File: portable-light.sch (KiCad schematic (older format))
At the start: 97 parts, among them J1 Conn_01x08, J2 Prog, Q1 MMBT2222A, Q2 MMBT2222A, Q3 MMBT2222A, Q4 MMBT2222A, Q5 MMBT2222A, Q6 PHD45N03LTA, Q7 PHD45N03LTA, Q8 MMBT2222A, U1 ATmega88PA-AU, U2 L78L05_SOT89, U3 LTC1733EMSEPBF, X1 LOAD, Y1 Crystal

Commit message: Schematics and PCB layout complete
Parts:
- removed C4: 100n, Capacitor_SMD:C_1206_3216Metric_Pad1.42x1.75mm_HandSolder, symbol Device:C_Small
- removed R26: 1MEG, Resistor_THT:R_Axial_DIN0309_L9.0mm_D3.2mm_P12.70mm_Horizontal, symbol Device:R_Small
- added J3: Charger, Connector_PinHeader_2.54mm:PinHeader_1x02_P2.54mm_Vertical, symbol Connector_Generic:Conn_01x02
- added JP1: Jumper_2_Open, Jumper:SolderJumper-2_P1.3mm_Open_RoundedPad1.0x1.5mm, symbol Jumper:Jumper_2_Open
- added NT1, NT2: Net-Tie_2, NetTie:NetTie-2_SMD_Pad0.5mm, symbol Device:Net-Tie_2
- BT1: footprint Connector_PinHeader_1.00mm:PinHeader_1x02_P1.00mm_Vertical -> Connector_PinHeader_2.54mm:PinHeader_1x02_P2.54mm_Vertical
- C4: renamed from C5; value 100n -> 330n
- R25: value 1MEG -> 500K
- renumbered C11 to C10, C12 to C11, C13 to C12, C14 to C13, C15 to C14, C16 to C15, C17 to C16, C18 to C17, C20 to C18, C21 to C19, C19 to C20, C23 to C21, C24 to C23, C25 to C24, C26 to C25, C6 to C5, C7 to C6, C8 to C7, C9 to C8, C10 to C9, X1 to J4, JP1 to JP2, R27 to R26, R28 to R27, R29 to R28, R30 to R29, R31 to R30, R32 to R31, R33 to R32, R34 to R33, R35 to R34, R36 to R35, R37 to R36, R38 to R37, R39 to R38, R40 to R39, R41 to R40, R42 to R41, R43 to R42, R44 to R43
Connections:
- net +BATT: now also U3.8 (SEL)
- net GND: now also NT1.1, NT2.1; no longer C13.2, C14.2
- net GNDA: now also NT2.2
- net GNDPWR: now also C13.2, C14.2, J3.2 (Pin_2), NT1.2
- net VDC: now also J3.1 (Pin_1); no longer U3.8 (SEL)
- net high_mos: now also U1.1 (PD3); no longer J2.5 (Pin_5), U1.15 (PB3)
- net low_mos: now also JP1.2 (B); no longer U1.1 (PD3)
- net oc1a: now also U1.12 (PB0); no longer U1.13 (PB1)
- net prog_pulldown: now also U1.32 (PD2); no longer U1.31 (PD1)
- net prog_pullup: now also U1.31 (PD1); no longer U1.32 (PD2)
- net pump-in: now also U1.13 (PB1); no longer U1.12 (PB0)
- new net mosi: J2.5 (Pin_5), JP1.1 (A), U1.15 (PB3)
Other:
- note added: "Power"
- moved on the sheet: BT1, C1, C10, C11, C12, C13, C14, C15, C16, C17, C18, C19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

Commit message: commit before checkout
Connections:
- net +BATT: no longer U3.8 (SEL)
- net VDC: now also U3.8 (SEL)
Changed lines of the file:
@@
 L power:+BATT #PWR041
 U 1 1 5F1C71D9
-P 9800 1050
-F 0 "#PWR041" H 9800 900 50  0001 C CNN
-F 1 "+BATT" H 9800 1200 50  0000 C CNN
-F 2 "" H 9800 1050 50  0001 C CNN
-F 3 "" H 9800 1050 50  0001 C CNN
-	1    9800 1050
+P 9800 1300
+F 0 "#PWR041" H 9800 1150 50  0001 C CNN
+F 1 "+BATT" H 9800 1450 50  0000 C CNN
+F 2 "" H 9800 1300 50  0001 C CNN
+F 3 "" H 9800 1300 50  0001 C CNN
+	1    9800 1300
 	1    0    0    -1
 $EndComp
 Wire Wire Line
 	9300 1600 9800 1600
-Wire Wire Line
-	9800 1600 9800 1050
-Wire Wire Line
-	9550 1700 9550 1050
 Wire Wire Line
 	9300 1700 9550 1700
@@
 	3750 2400 3950 2400
 $Comp
-L power:+BATT #PWR040
-U 1 1 5F20B594
-P 9550 1050
-F 0 "#PWR040" H 9550 900 50  0001 C CNN
-F 1 "+BATT" H 9500 1200 50  0000 C CNN
-F 2 "" H 9550 1050 50  0001 C CNN
-F 3 "" H 9550 1050 50  0001 C CNN
-	1    9550 1050
-	1    0    0    -1
-$EndComp
-$Comp
 L Connector_Generic:Conn_01x02 J3
 U 1 1 5F22ABC0
@@
 Text Notes 4450 7500 0    157  ~ 31
 Power
+$Comp
+L power:VDC #PWR?
+U 1 1 5F1D8884
+P 9550 1300
+F 0 "#PWR?" H 9550 1200 50  0001 C CNN
+F 1 "VDC" H 9550 1450 50  0000 C CNN
+F 2 "" H 9550 1300 50  0001 C CNN
+F 3 "" H 9550 1300 50  0001 C CNN
+	1    9550 1300
+	1    0    0    -1
+$EndComp
+Wire Wire Line
+	9550 1700 9550 1300
+Wire Wire Line
+	9800 1600 9800 1300
 $EndSCHEMATC

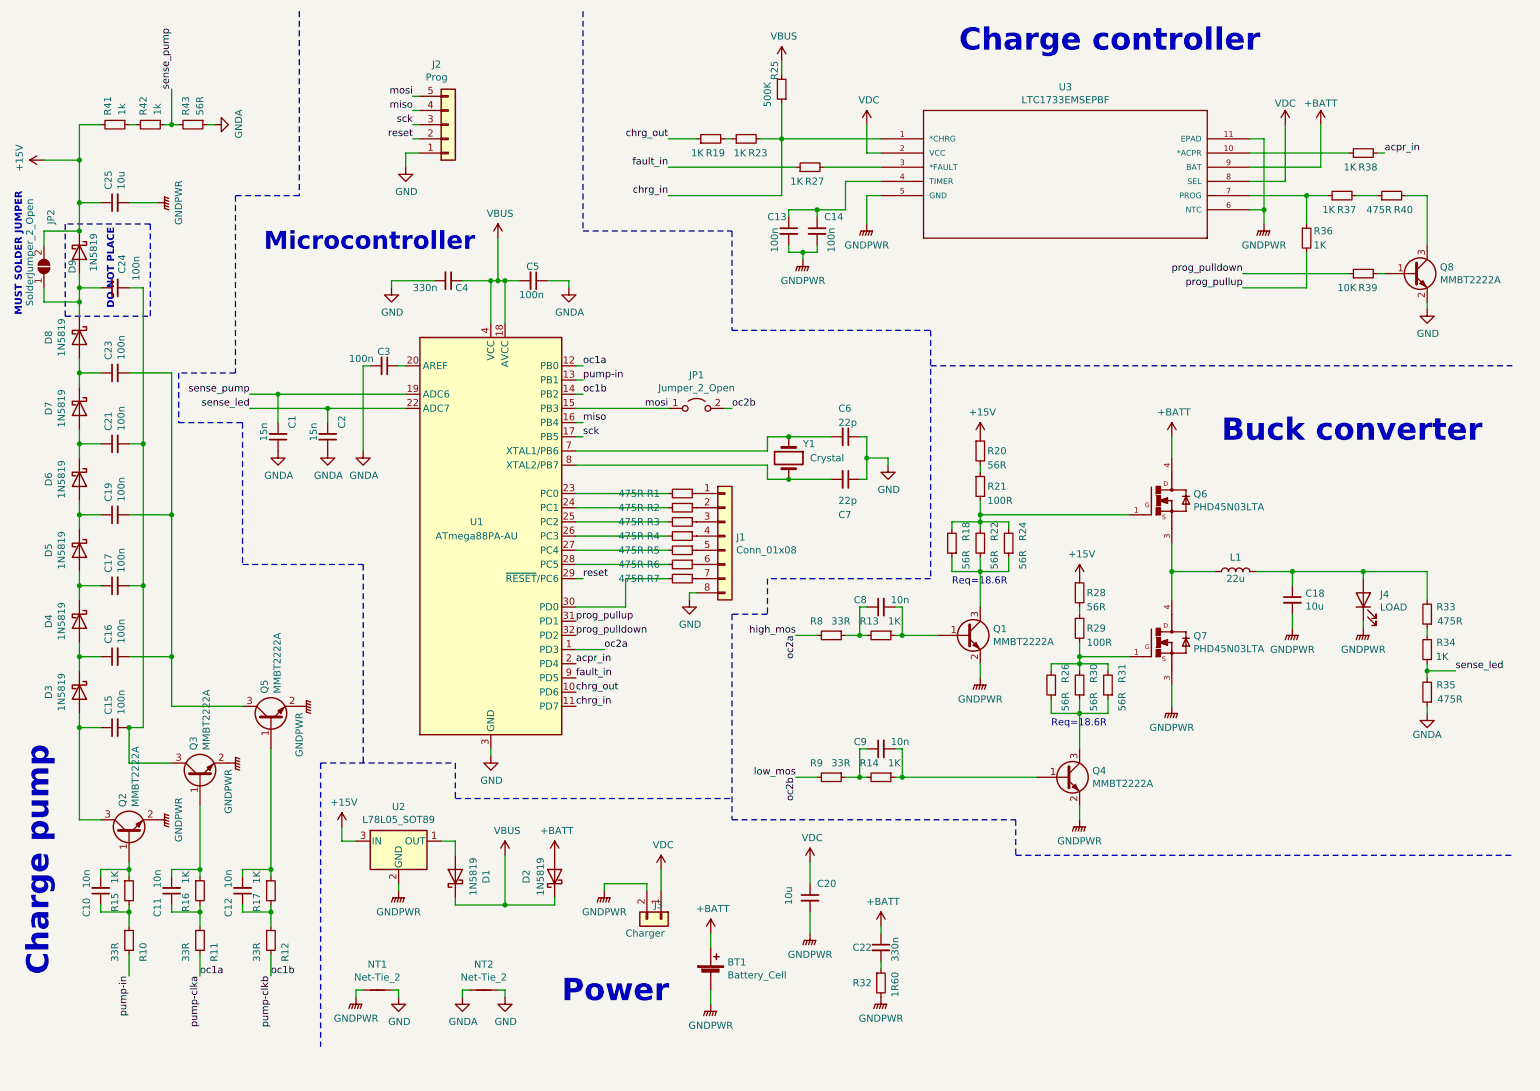
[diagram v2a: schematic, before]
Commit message: AVR Charge-pump bug fixed
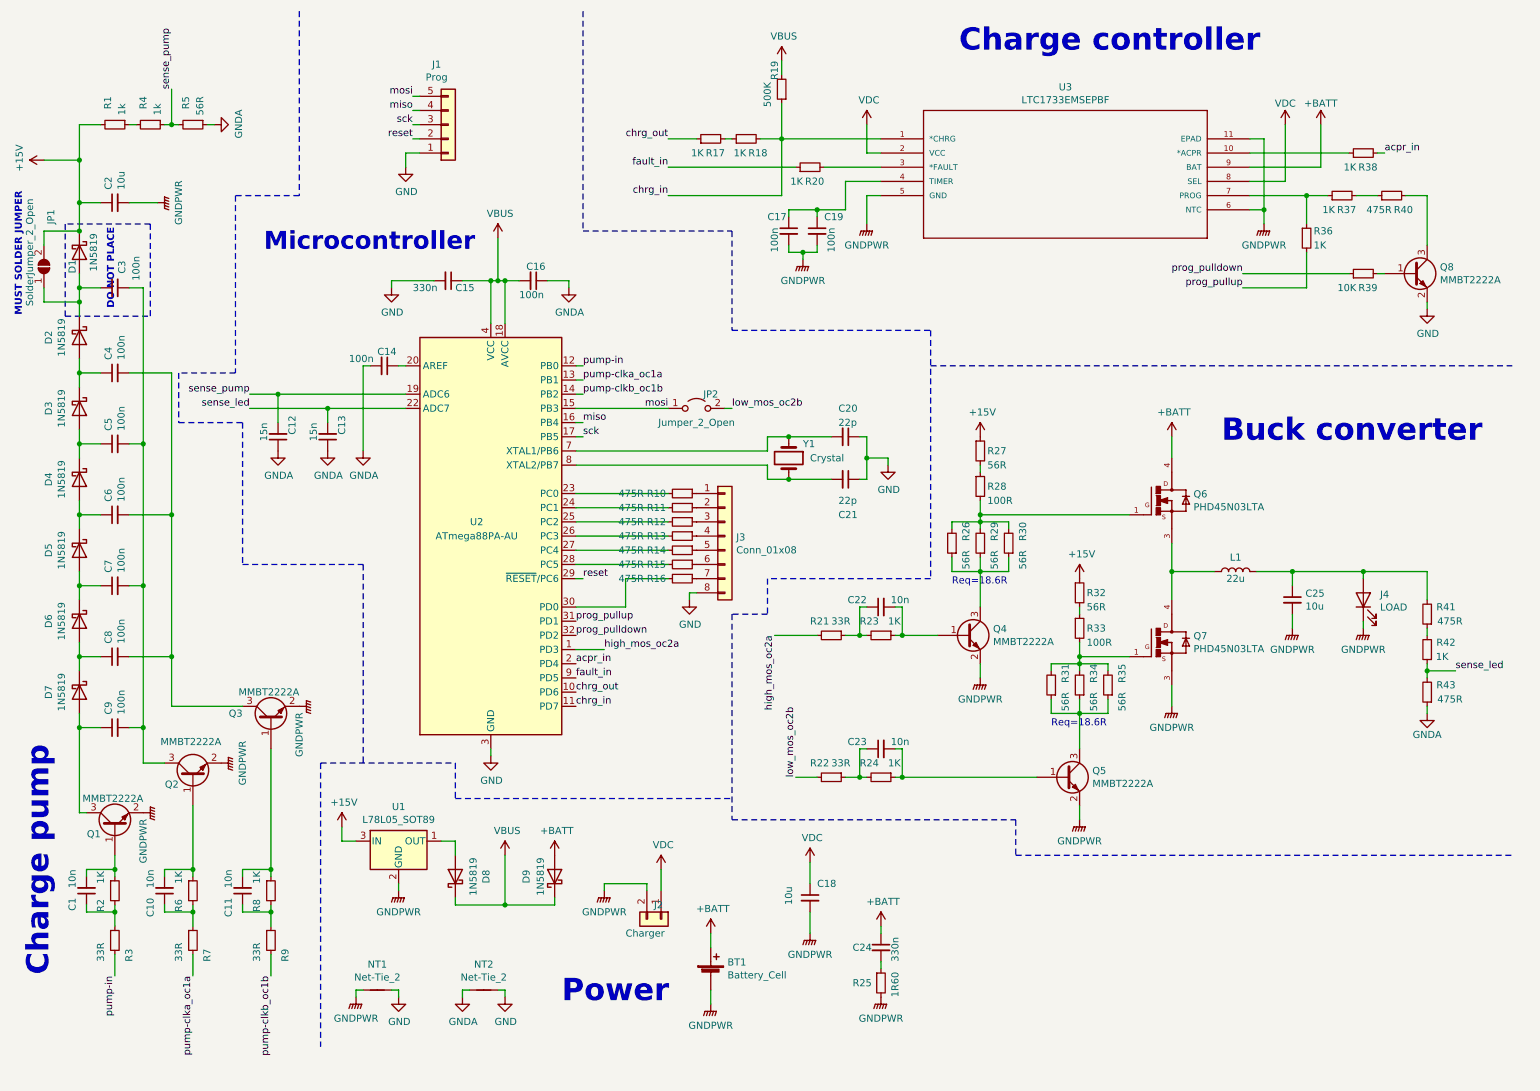
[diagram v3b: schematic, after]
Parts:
- renumbered C11 to C1, C12 to C11, C1 to C12, C2 to C13, C3 to C14, C4 to C15, C5 to C16, C13 to C17, C20 to C18, C14 to C19, C25 to C2, C6 to C20, C7 to C21, C8 to C22, C9 to C23, C22 to C24, C18 to C25, C24 to C3, C23 to C4, C21 to C5, C19 to C6, C17 to C7, C16 to C8, C15 to C9, D9 to D1, D8 to D2, D7 to D3, D6 to D4, D4 to D6, D3 to D7, D1 to D8, D2 to D9, J2 to J1, J3 to J2, J1 to J3, JP2 to JP1, JP1 to JP2, Q3 to Q1, Q5 to Q3, Q1 to Q4, Q4 to Q5, R41 to R1, R1 to R10, R2 to R11, R3 to R12, R4 to R13, R5 to R14, R6 to R15, R7 to R16, R19 to R17, R23 to R18, R25 to R19, R16 to R2, R27 to R20, R8 to R21, R9 to R22, R13 to R23, R14 to R24, R32 to R25, R18 to R26, R20 to R27, R21 to R28, R22 to R29, R11 to R3, R24 to R30, R26 to R31, R28 to R32, R29 to R33, R30 to R34, R31 to R35, R42 to R4, R33 to R41, R34 to R42, R35 to R43, R43 to R5, R15 to R6, R10 to R7, R17 to R8, R12 to R9, U2 to U1, U1 to U2
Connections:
- net oc1a is gone; now on net pump-in: R3.2, U2.12 (PB0)
- net pump-in: no longer R7.2, U2.13 (PB1)
- net at C9.1, D7.2 (A): now also Q1.3 (C); no longer Q2.3 (C)
- net at C3.2, C5.2, C7.2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: now also Q2.3 (C); no longer Q1.3 (C)
- net high_mos renamed high_mos_oc2a
- net low_mos renamed low_mos_oc2b
- net oc1b renamed pump-clkb_oc1b
- new net pump-clka_oc1a: R7.2, U2.13 (PB1)
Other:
- moved on the sheet: C1, C10, Q1, Q2, R2, R3, R6, R7

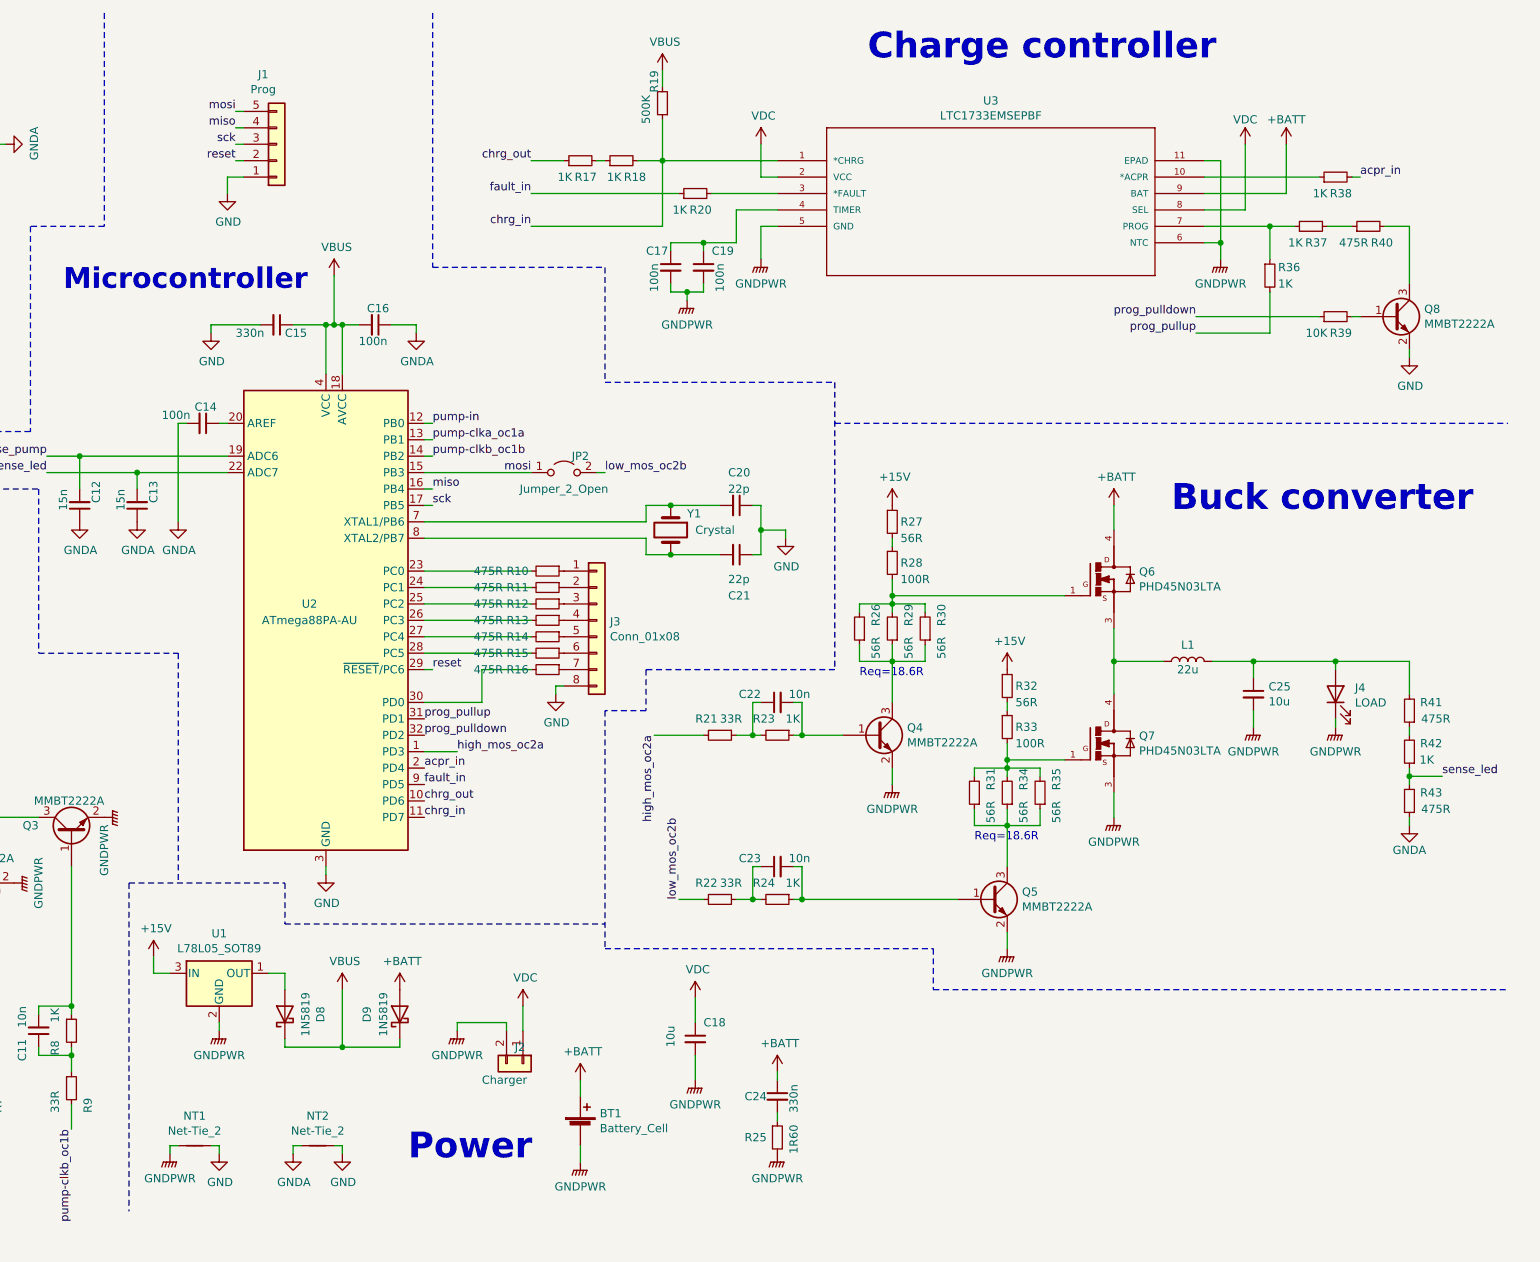
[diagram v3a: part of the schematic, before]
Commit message: Added push-button
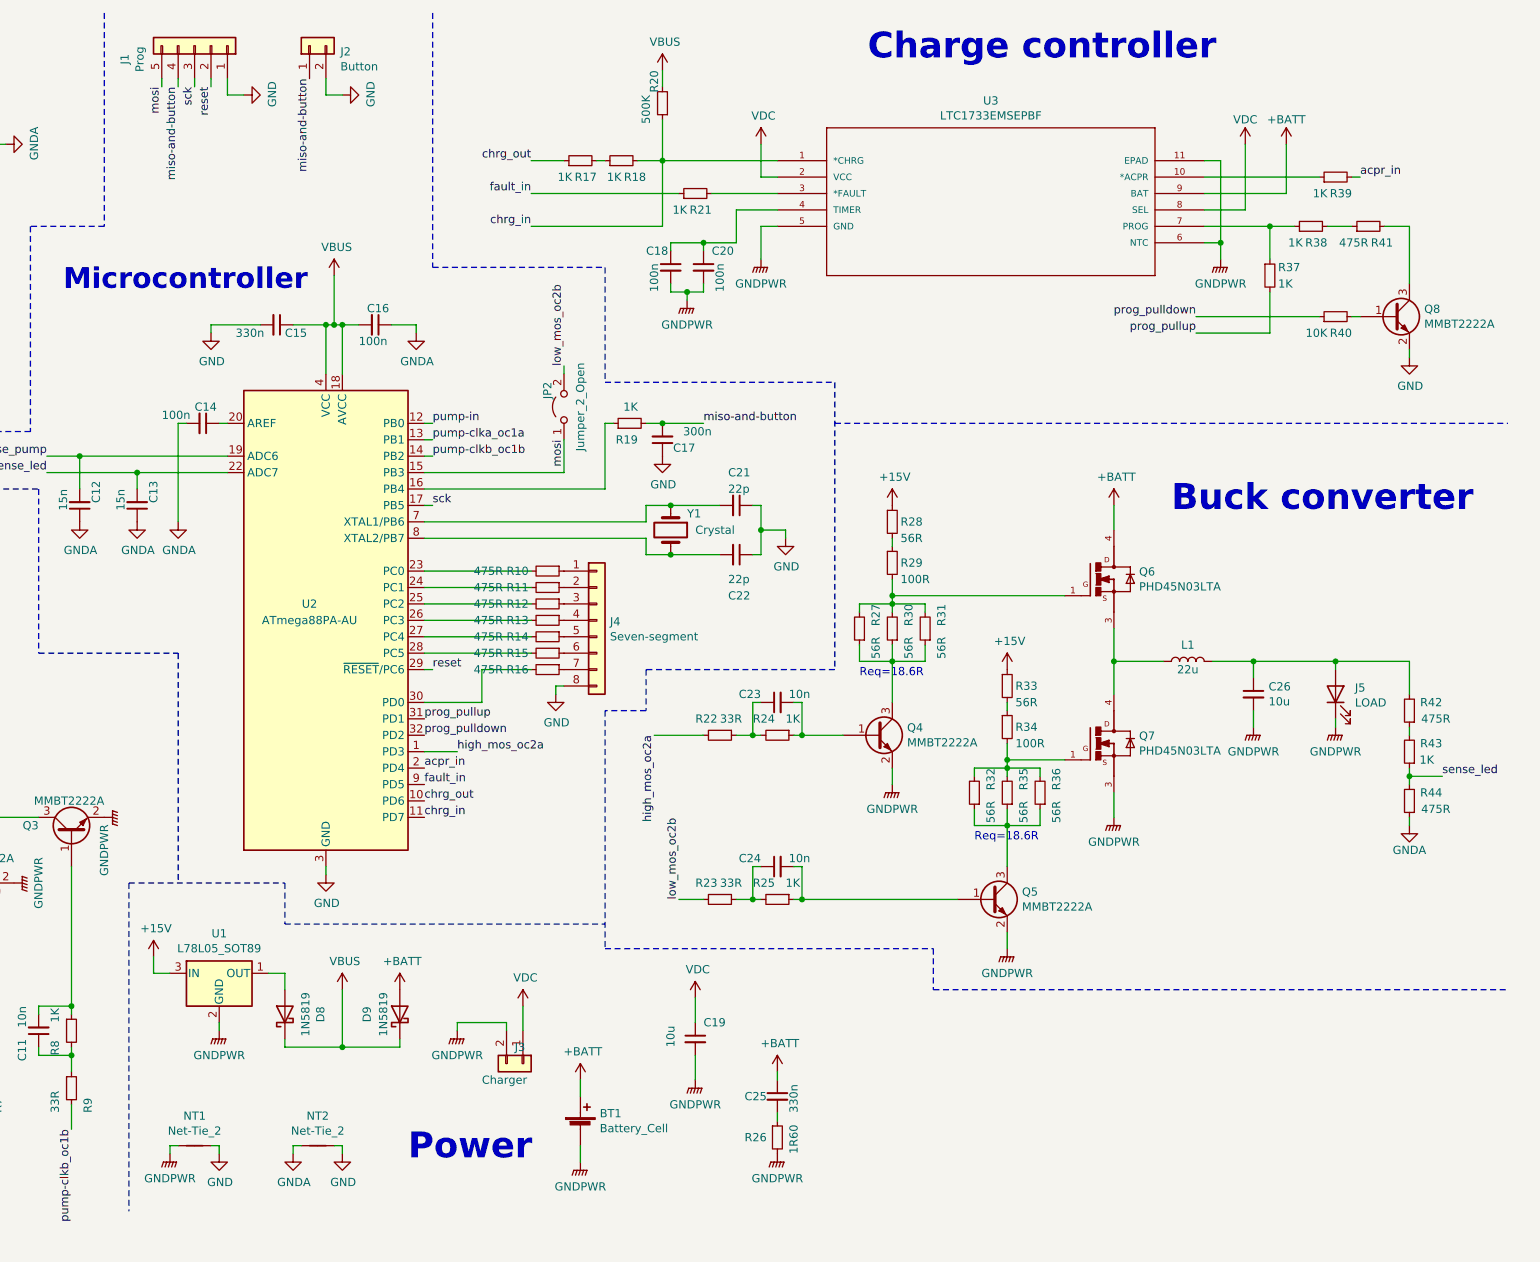
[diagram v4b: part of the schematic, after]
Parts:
- added C17: 300n, Capacitor_SMD:C_0805_2012Metric_Pad1.15x1.40mm_HandSolder, symbol Device:C_Small
- added J2: Button, Ribbon_Cable:Ribbon_2, symbol Connector_Generic:Conn_01x02
- added R19: 1K, Resistor_SMD:R_0603_1608Metric_Pad1.05x0.95mm_HandSolder, symbol Device:R_Small
- J4: renamed from J3; value Conn_01x08 -> Seven-segment
- renumbered C17 to C18, C18 to C19, C19 to C20, C20 to C21, C21 to C22, C22 to C23, C23 to C24, C24 to C25, C25 to C26, J2 to J3, J4 to J5, R19 to R20, R20 to R21, R21 to R22, R22 to R23, R23 to R24, R24 to R25, R25 to R26, R26 to R27, R27 to R28, R28 to R29, R29 to R30, R30 to R31, R31 to R32, R32 to R33, R33 to R34, R34 to R35, R35 to R36, R36 to R37, R37 to R38, R38 to R39, R39 to R40, R40 to R41, R41 to R42, R42 to R43, R43 to R44
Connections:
- net GND: now also C17.1, J2.2 (Pin_2)
- net miso: no longer names the net of U2.16 (PB4)
- net miso: now also R19.1; no longer J1.4 (Pin_4)
- new net miso-and-button: C17.2, J1.4 (Pin_4), J2.1 (Pin_1), R19.2
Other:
- moved on the sheet: J1, JP2

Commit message: First review and refactoring complete; PCB is ready
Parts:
- removed C15: 330n, Capacitor_SMD:C_1206_3216Metric_Pad1.42x1.75mm_HandSolder, symbol Device:C_Small
- added C16: 300n, Capacitor_SMD:C_0805_2012Metric_Pad1.15x1.40mm_HandSolder, symbol Device:C_Small
- added C17, C2: 100n, Capacitor_SMD:C_1206_3216Metric_Pad1.42x1.75mm_HandSolder, symbol Device:C_Small
- renumbered C9 to C10, C10 to C11, C11 to C12, C12 to C13, C13 to C14, C14 to C15, C16 to C18, C17 to C19, C18 to C20, C19 to C21, C20 to C22, C21 to C23, C22 to C24, C23 to C25, C24 to C26, C25 to C27, C26 to C28, C2 to C3, C3 to C4, C4 to C5, C5 to C6, C6 to C7, C7 to C8, C8 to C9
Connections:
- net +15V: now also C2.1
- net GND: now also C16.1
- net GNDPWR: now also C17.2, C2.2
- net VBUS: now also C16.2
- net at D8.2 (A), U1.1 (OUT): now also C17.1
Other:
- moved on the sheet: BT1, D8, D9, J3, NT2, R1, R4, R5, U1
